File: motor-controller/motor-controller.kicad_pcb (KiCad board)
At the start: 2 copper layers, 16 parts, among them J1 Molex 172043-0201 R/A, J2 Molex 172043-0302 R/A, J3 MCU-IO, U1 DRV10983PWP

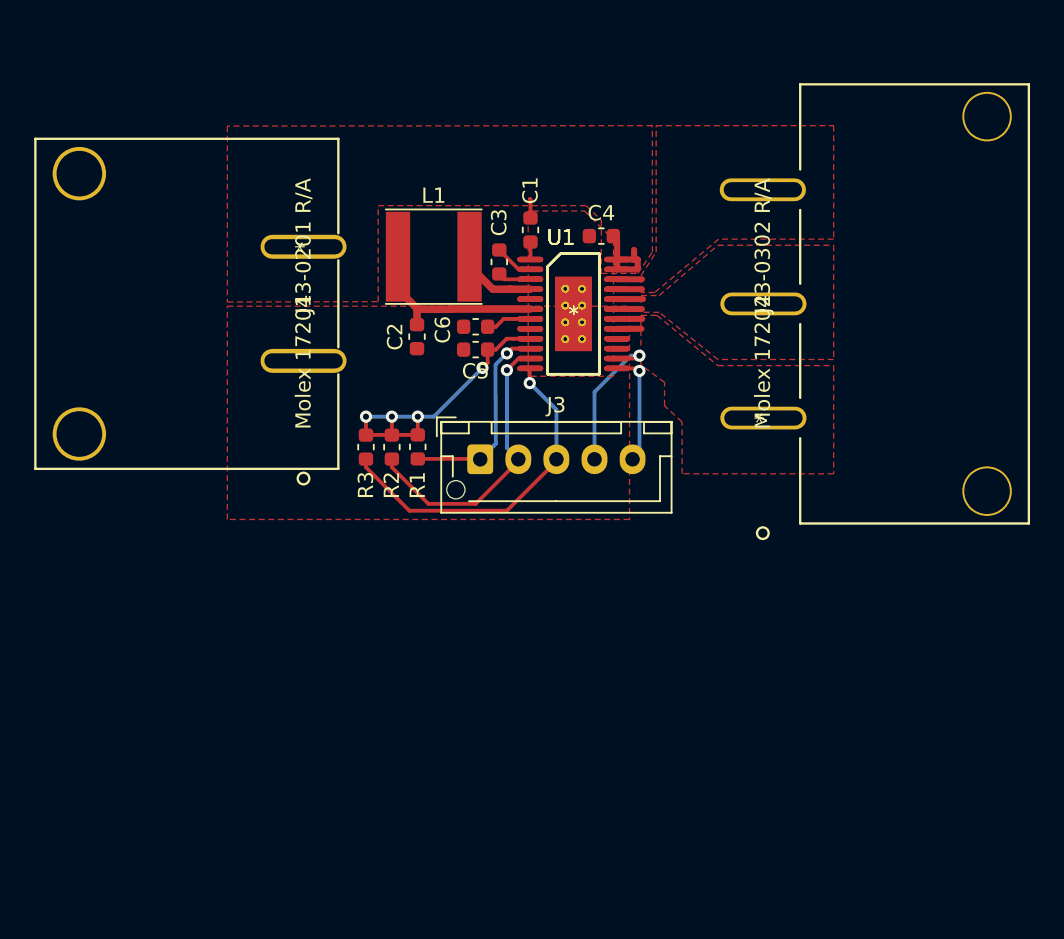
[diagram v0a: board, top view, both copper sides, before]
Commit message: Added ground planes, thermal vias
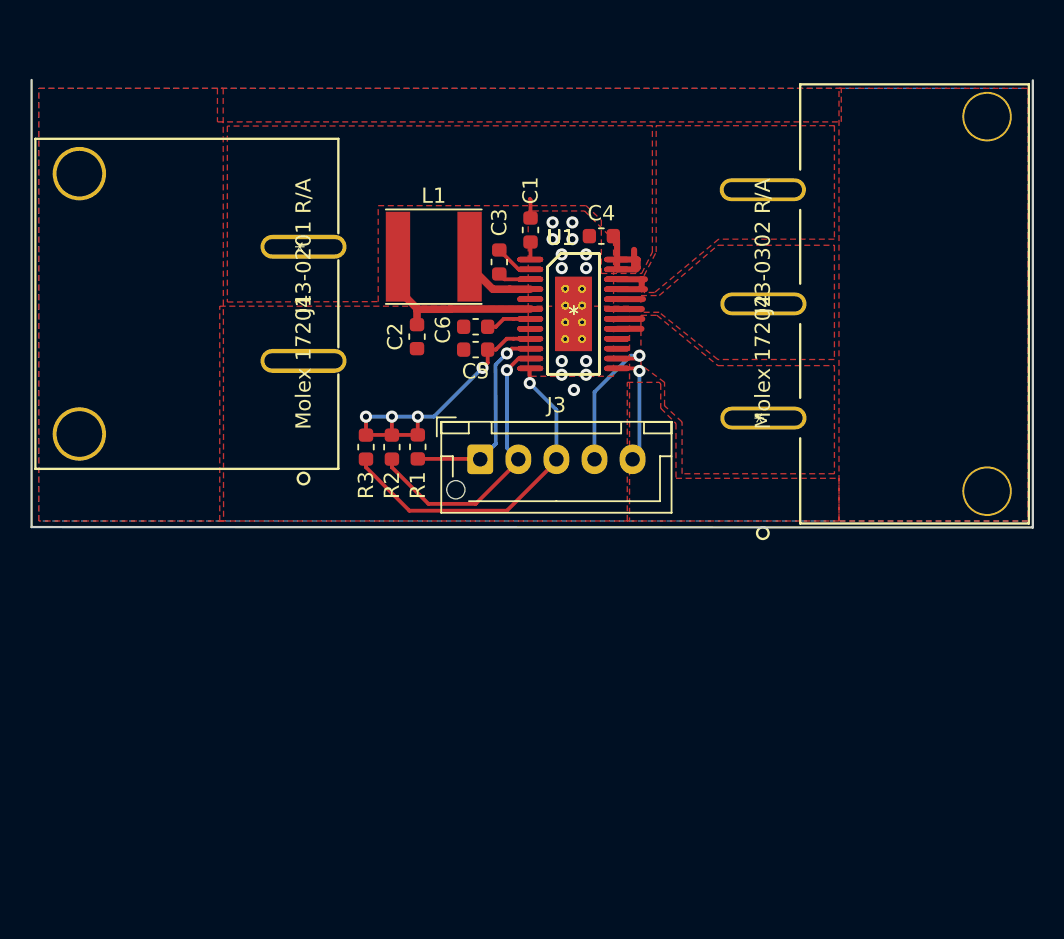
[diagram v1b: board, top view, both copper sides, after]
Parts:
- removed the U1 at (152.4, 103.5) (x3)
- added U1 (x3): DRV10983PWP, custom:PWP0024B, F.Cu at (152.4, 103.5)
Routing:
- net Net-(J2-Pad3): track 3.26 -> 4.31 mm
- net GND: vias 0 -> 13
- added copper zone on B.Cu, net GND
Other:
- board outline added: 65.7 x 29.4 mm
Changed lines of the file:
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@@
   (general
     (thickness 1.6)
-    (drawings 5)
-    (tracks 98)
+    (drawings 8)
+    (tracks 115)
     (zones 0)
     (modules 16)
@@
     (pad 4 thru_hole circle (at -4.8006 14.7193 180) (size 3.2512 3.2512) (drill 2.9972) (layers *.Cu *.Mask))
   )
+  (gr_line (start 116.8 88.15) (end 116.8 117.5) (layer Edge.Cuts) (width 0.15))
+  (gr_line (start 182.525 88.175) (end 182.525 117.525) (layer Edge.Cuts) (width 0.15))
+  (gr_line (start 182.525 117.525) (end 116.8 117.5) (layer Edge.Cuts) (width 0.15))
   (gr_line (start 161.95 106.5) (end 161.95 99) (layer Dwgs.User) (width 0.2))
   (gr_line (start 167.65 106.5) (end 161.95 106.5) (layer Dwgs.User) (width 0.2))
@@
   (segment (start 155.233726 99.935001) (end 156.35 99.935001) (width 0.4) (layer F.Cu) (net 2))
   (segment (start 155.233726 100.585002) (end 156.483725 100.585002) (width 0.4) (layer F.Cu) (net 2))
+  (segment (start 156.35 99.935001) (end 156.35 100.4) (width 0.4) (layer F.Cu) (net 2))
   (segment (start 142.15 103.2) (end 140.85 101.9) (width 0.5) (layer F.Cu) (net 3))
   (segment (start 144.270004 103.2) (end 142.15 103.2) (width 0.5) (layer F.Cu) (net 3))
@@
   (segment (start 142.1 103.25) (end 142.1 104.2125) (width 0.5) (layer F.Cu) (net 3))
   (segment (start 142.15 103.2) (end 142.1 103.25) (width 0.5) (layer F.Cu) (net 3))
+  (via (at 151.6 100.5) (size 0.8) (drill 0.4) (layers F.Cu B.Cu) (net 4))
+  (via (at 153.2 100.5) (size 0.8) (drill 0.4) (layers F.Cu B.Cu) (net 4))
+  (via (at 151.6 99.6) (size 0.8) (drill 0.4) (layers F.Cu B.Cu) (net 4))
+  (via (at 153.2 99.6) (size 0.8) (drill 0.4) (layers F.Cu B.Cu) (net 4))
+  (via (at 151.6 106.6) (size 0.8) (drill 0.4) (layers F.Cu B.Cu) (net 4))
+  (via (at 151.6 107.5) (size 0.8) (drill 0.4) (layers F.Cu B.Cu) (net 4))
+  (via (at 153.2 107.5) (size 0.8) (drill 0.4) (layers F.Cu B.Cu) (net 4))
+  (via (at 153.2 106.6) (size 0.8) (drill 0.4) (layers F.Cu B.Cu) (net 4))
+  (via (at 151 97.5) (size 0.8) (drill 0.4) (layers F.Cu B.Cu) (net 4))
+  (via (at 151 98.6) (size 0.8) (drill 0.4) (layers F.Cu B.Cu) (net 4))
+  (via (at 152.3 98.6) (size 0.8) (drill 0.4) (layers F.Cu B.Cu) (net 4))
+  (via (at 152.3 97.5) (size 0.8) (drill 0.4) (layers F.Cu B.Cu) (net 4))
+  (via (at 152.4 108.5) (size 0.8) (drill 0.4) (layers F.Cu B.Cu) (net 4))
   (segment (start 147.847501 101.235001) (end 149.533728 101.235001) (width 0.25) (layer F.Cu) (net 5))
   (segment (start 147.5 100.8875) (end 147.847501 101.235001) (width 0.25) (layer F.Cu) (net 5))
@@
   (segment (start 155.233726 102.535001) (end 156.935001 102.535001) (width 0.4) (layer F.Cu) (net 9))
   (segment (start 155.233726 103.185002) (end 156.864998 103.185002) (width 0.4) (layer F.Cu) (net 9))
-  (segment (start 155.233726 101.235001) (end 156.864999 101.235001) (width 0.4) (layer F.Cu) (net 10))
-  (segment (start 155.233726 101.885002) (end 156.864998 101.885002) (width 0.4) (layer F.Cu) (net 10))
+  (segment (start 156.85 101.235001) (end 156.85 101.885002) (width 0.4) (layer F.Cu) (net 10))
+  (segment (start 156.85 101.885002) (end 157.064998 101.885002) (width 0.4) (layer F.Cu) (net 10))
+  (segment (start 155.233726 101.885002) (end 156.85 101.885002) (width 0.4) (layer F.Cu) (net 10))
+  (segment (start 156.85 101.235001) (end 157.064999 101.235001) (width 0.4) (layer F.Cu) (net 10))
+  (segment (start 155.233726 101.235001) (end 156.85 101.235001) (width 0.4) (layer F.Cu) (net 10))
   (via (at 148 106.1) (size 0.8) (drill 0.4) (layers F.Cu B.Cu) (net 11))
   (segment (start 146.225 113.025) (end 146.25 113.05) (width 0.25) (layer F.Cu) (net 11))
@@
     (polygon
       (pts
-        (xy 156.8 102.3) (xy 158 102.3) (xy 161.85 99) (xy 169.45 99) (xy 169.45 106.5)
+        (xy 156.8 102.3) (xy 158 102.3) (xy 161.85 99) (xy 169.5 99) (xy 169.5 106.5)
         (xy 161.85 106.5) (xy 158 103.4) (xy 156.8 103.4)
       )
@@
       (pts
         (xy 129.65 91.175) (xy 129.65 102.725) (xy 139.55 102.7) (xy 139.55 96.4) (xy 153.2 96.4)
-        (xy 154.2 97.35) (xy 154.2 100.85) (xy 156.6 100.85) (xy 157.55 99.45) (xy 157.55 91.15)
+        (xy 154.2 97.35) (xy 154.2 100.85) (xy 156.85 100.85) (xy 157.55 99.45) (xy 157.55 91.15)
       )
     )
@@
     (polygon
       (pts
-        (xy 156.8 102.1) (xy 156.8 101) (xy 157.8 99.45) (xy 157.8 91.15) (xy 169.45 91.15)
-        (xy 169.45 98.6) (xy 161.9 98.6) (xy 157.7 102.1)
+        (xy 157 102.1) (xy 157 101) (xy 157.8 99.45) (xy 157.8 91.15) (xy 169.5 91.15)
+        (xy 169.5 98.6) (xy 161.9 98.6) (xy 157.7 102.1)
       )
     )
@@
       (pts
         (xy 159.5 110.6) (xy 158.35 109.5375) (xy 158.35 108) (xy 156.8 106.85) (xy 156.8 103.6)
-        (xy 157.85 103.6) (xy 161.85 106.9) (xy 169.45 106.9) (xy 169.45 114) (xy 159.5 114)
+        (xy 157.85 103.6) (xy 161.85 106.9) (xy 169.5 106.9) (xy 169.5 114) (xy 159.5 114)
       )
     )
@@
     (polygon
       (pts
-        (xy 156.05 103) (xy 156.05 117) (xy 129.65 117) (xy 129.65 103)
+        (xy 156.05 103) (xy 156.05 117.1) (xy 129.15 117.1) (xy 129.15 103)
       )
     )
@@
       )
     )
+  )
+  (zone (net 4) (net_name GND) (layer F.Cu) (hatch edge 0.508)
+    (connect_pads (clearance 0.25))
+    (min_thickness 0.254)
+    (fill yes (arc_segments 16) (thermal_gap 0.508) (thermal_bridge_width 0.508))
+    (polygon
+      (pts
+        (xy 155.9 108) (xy 158 108) (xy 158.1 108.1) (xy 158.1 109.7) (xy 159.1 110.7)
+        (xy 159.1 114.3) (xy 169.8 114.3) (xy 169.8 117.1) (xy 155.9 117.1)
+      )
+    )
+  )
+  (zone (net 4) (net_name GND) (layer F.Cu) (hatch edge 0.508)
+    (connect_pads (clearance 0.25))
+    (min_thickness 0.254)
+    (fill yes (arc_segments 16) (thermal_gap 0.508) (thermal_bridge_width 0.508))
+    (polygon
+      (pts
+        (xy 169.8 117) (xy 169.8 88.7) (xy 182.2 88.7) (xy 182.2 117.1) (xy 169.8 117.1)
+      )
+    )
+  )
+  (zone (net 4) (net_name GND) (layer F.Cu) (hatch edge 0.508)
+    (connect_pads (clearance 0.25))
+    (min_thickness 0.254)
+    (fill yes (arc_segments 16) (thermal_gap 0.508) (thermal_bridge_width 0.508))
+    (polygon
+      (pts
+        (xy 129.4 117.1) (xy 117.275 117.1) (xy 117.275 88.7) (xy 129.375 88.7)
+      )
+    )
+  )
+  (zone (net 4) (net_name GND) (layer F.Cu) (hatch edge 0.508)
+    (connect_pads (clearance 0.25))
+    (min_thickness 0.254)
+    (fill yes (arc_segments 16) (thermal_gap 0.508) (thermal_bridge_width 0.508))
+    (polygon
+      (pts
+        (xy 169.95 90.9) (xy 169.95 88.7) (xy 129 88.7) (xy 129 90.9)
+      )
+    )
+  )
+  (zone (net 4) (net_name GND) (layer B.Cu) (hatch edge 0.508)
+    (connect_pads (clearance 0.25))
+    (min_thickness 0.254)
+    (fill yes (arc_segments 16) (thermal_gap 0.508) (thermal_bridge_width 0.508))
+    (polygon
+      (pts
+        (xy 117.275 88.7) (xy 182.2 88.7) (xy 182.2 117.1) (xy 117.3 117.1) (xy 117.275 117.1)
+      )
+    )

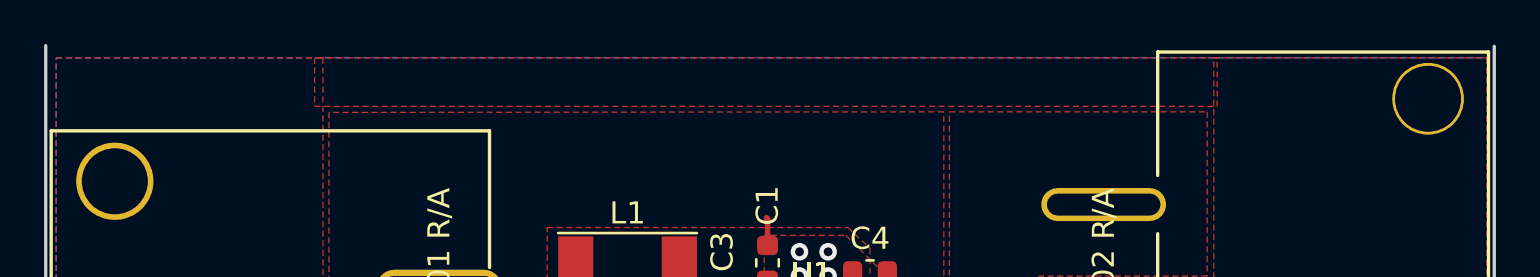
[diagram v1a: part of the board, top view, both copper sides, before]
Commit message: Added back top edge cut
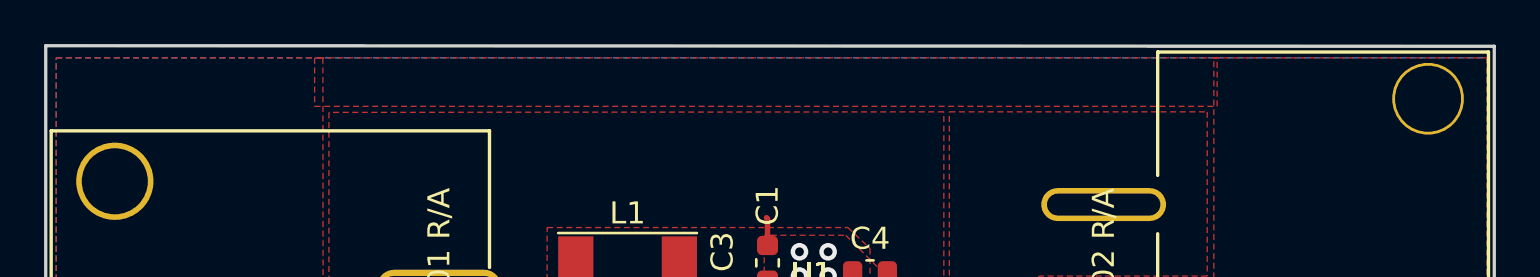
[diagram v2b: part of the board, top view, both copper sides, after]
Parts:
- removed the U1 at (152.4, 103.5) (x3)
- added U1 (x3): DRV10983PWP, custom:PWP0024B, F.Cu at (152.4, 103.5)
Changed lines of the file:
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@@
   (general
     (thickness 1.6)
-    (drawings 8)
+    (drawings 9)
     (tracks 115)
     (zones 0)
@@
     (33 F.Adhes user)
     (34 B.Paste user)
-    (35 F.Paste user hide)
+    (35 F.Paste user)
     (36 B.SilkS user)
     (37 F.SilkS user)
@@
     (pad 4 thru_hole circle (at -4.8006 14.7193 180) (size 3.2512 3.2512) (drill 2.9972) (layers *.Cu *.Mask))
   )
+  (gr_line (start 182.525 88.175) (end 116.8 88.15) (layer Edge.Cuts) (width 0.15))
   (gr_line (start 116.8 88.15) (end 116.8 117.5) (layer Edge.Cuts) (width 0.15))
   (gr_line (start 182.525 88.175) (end 182.525 117.525) (layer Edge.Cuts) (width 0.15))

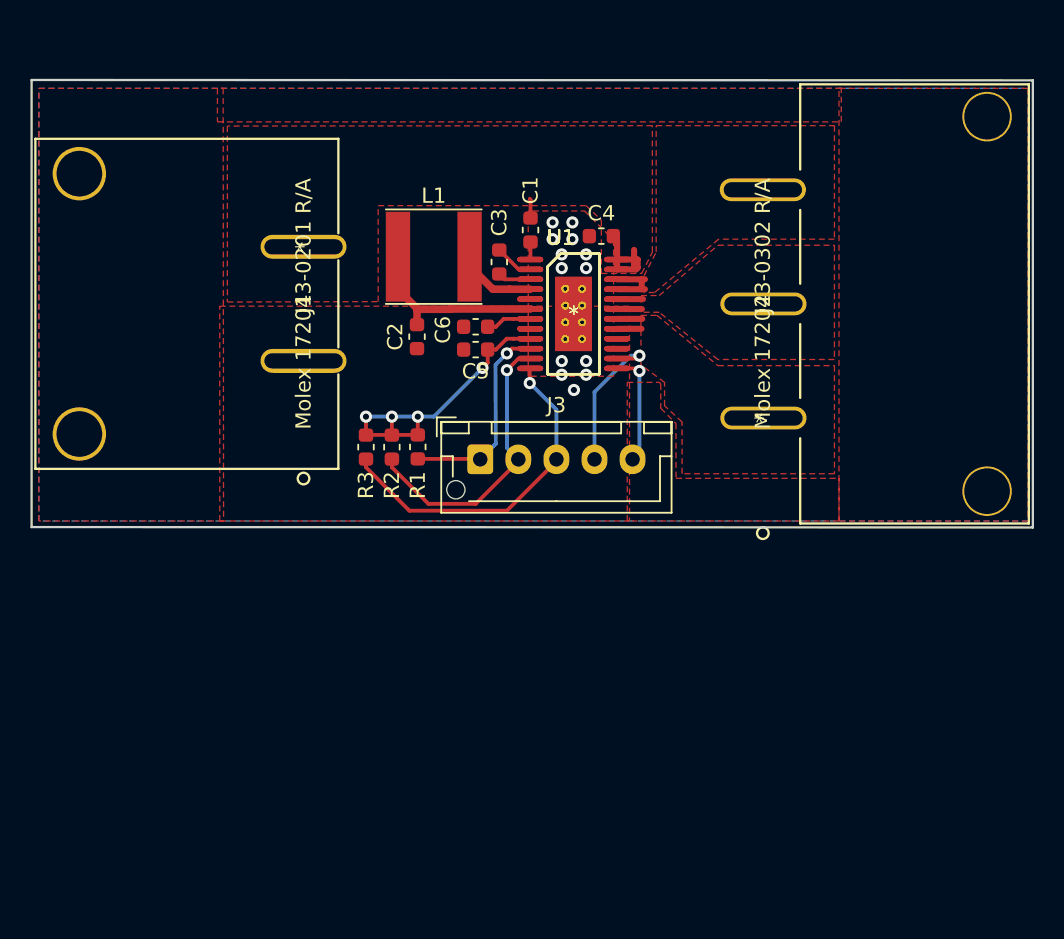
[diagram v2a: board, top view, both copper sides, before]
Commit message: Added fuse holder and modified position of mounting holes
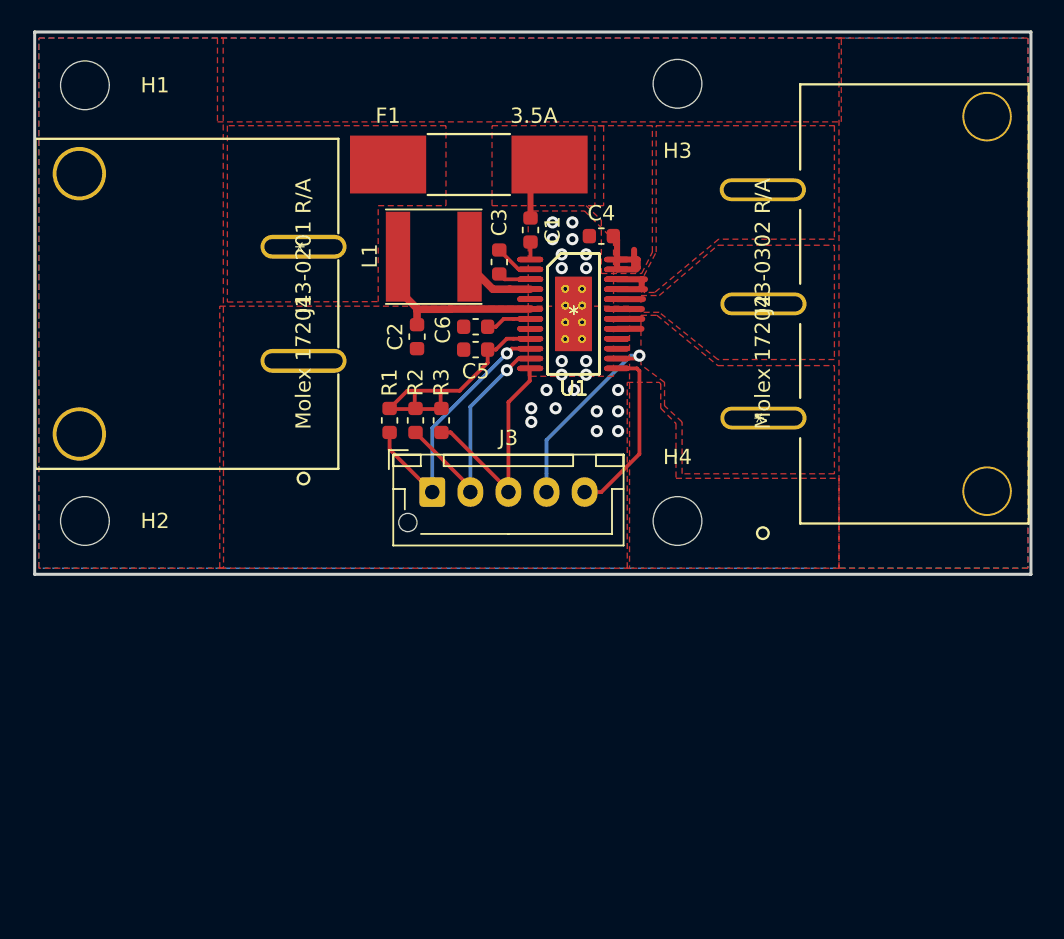
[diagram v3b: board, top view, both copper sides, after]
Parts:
- removed the U1 at (152.4, 103.5) (x3)
- added F1: 3.5A, custom:littelfuse-01110505Z-5x15mm, F.Cu at (145.5, 93.7)
- added H1: MountingHole, MountingHole:MountingHole_3.2mm_M3, F.Cu at (120.3, 88.5)
- added H2: MountingHole, MountingHole:MountingHole_3.2mm_M3, F.Cu at (120.3, 117.1)
- added H3: MountingHole, MountingHole:MountingHole_3.2mm_M3, F.Cu at (159.2, 88.4)
- added H4: MountingHole, MountingHole:MountingHole_3.2mm_M3, F.Cu at (159.2, 117.1)
- added U1 (x3): DRV10983PWP, custom:PWP0024B, F.Cu at (152.4, 103.5)
- moved R3 5.25 mm to (143.7, 110.5)
- moved J3 3.81 mm to (143.1, 115.2)
- moved R1 2.54 mm to (140.3, 110.5)
- moved R2 2.34 mm to (142.0, 110.5)
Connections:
- J1 pad 2: VCC -> Net-(F1-Pad1)
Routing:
- net Net-(J3-Pad3): track 22.4 -> 14.8 mm, vias 1 -> 0
- net Net-(J3-Pad1): track 13.4 -> 17.9 mm
- net /SPEED: track 7.52 -> 11.6 mm, vias 1 -> 0
- net /DIR: track 9.90 -> 13.4 mm
- net +3V3: track 20.4 -> 17.5 mm, vias 4 -> 0
- net Net-(J3-Pad2): track 19.3 -> 16.4 mm
- net VCC: track 7.96 -> 10.7 mm
- net GND: vias 13 -> 22
- added copper zone on F.Cu, net Net-(F1-Pad1)
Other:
- board size 65.7 x 29.4 mm -> 65.4 x 35.6 mm

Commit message: Adjusted copper pours; reroute I2C and other digital signal traces
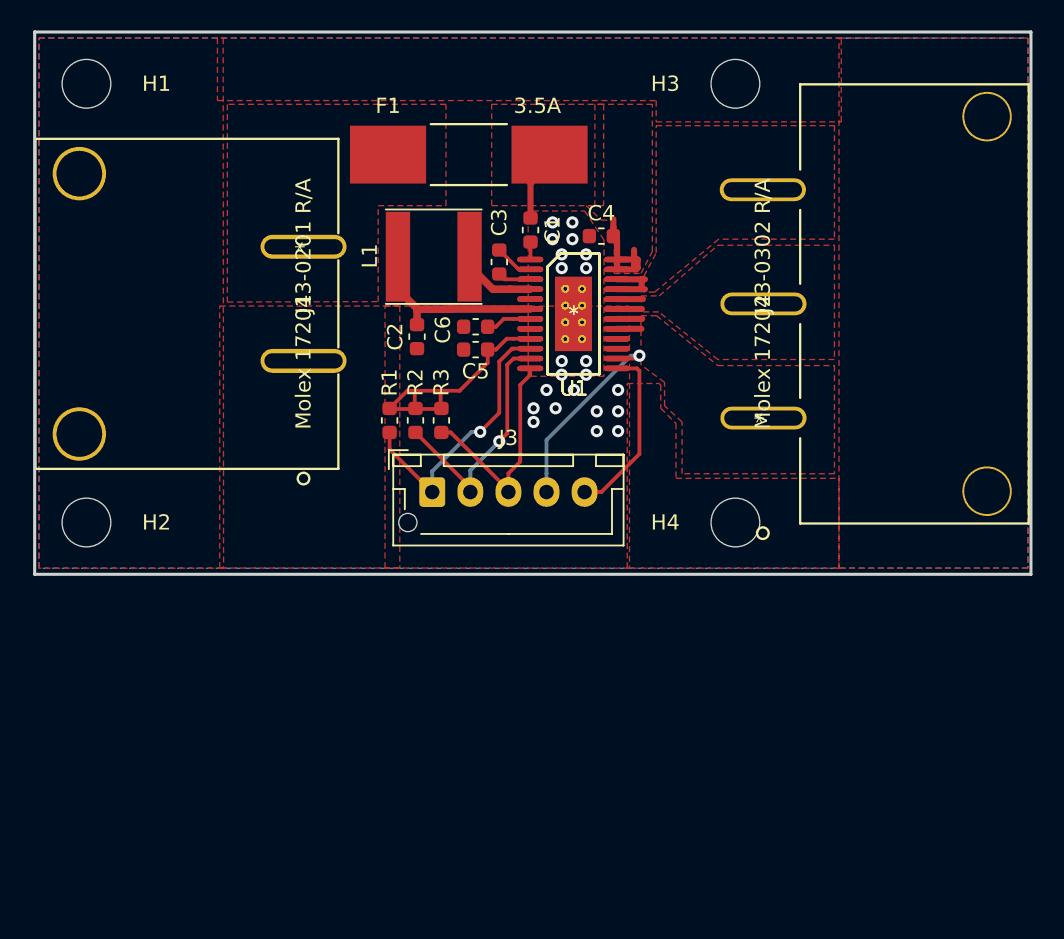
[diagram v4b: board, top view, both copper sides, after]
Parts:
- removed the U1 at (152.4, 103.5) (x3)
- added U1 (x3): DRV10983PWP, custom:PWP0024B, F.Cu at (152.4, 103.5)
- moved H4 3.80 mm to (163.0, 117.2)
- moved H3 3.80 mm to (163.0, 88.4)
- moved F1 0.65 mm to (145.5, 93.0)
- moved H2 0.14 mm to (120.4, 117.2)
- moved H1 0.14 mm to (120.4, 88.4)
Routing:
- net VCC: track 10.7 -> 11.8 mm
